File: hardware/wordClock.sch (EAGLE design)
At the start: 38 parts, among them J1 SPI_PRG, Q1 MOSFET-PCHANNELSMD, Q2 MOSFET-PCHANNELSMD, Q3 MOSFET-PCHANNELSMD, Q4 MOSFET-PCHANNELSMD, Q5 MOSFET-PCHANNELSMD, Q6 MOSFET-PCHANNELSMD, Q7 MOSFET-PCHANNELSMD, Q8 MOSFET-PCHANNELSMD, U2 TLC5940-NT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

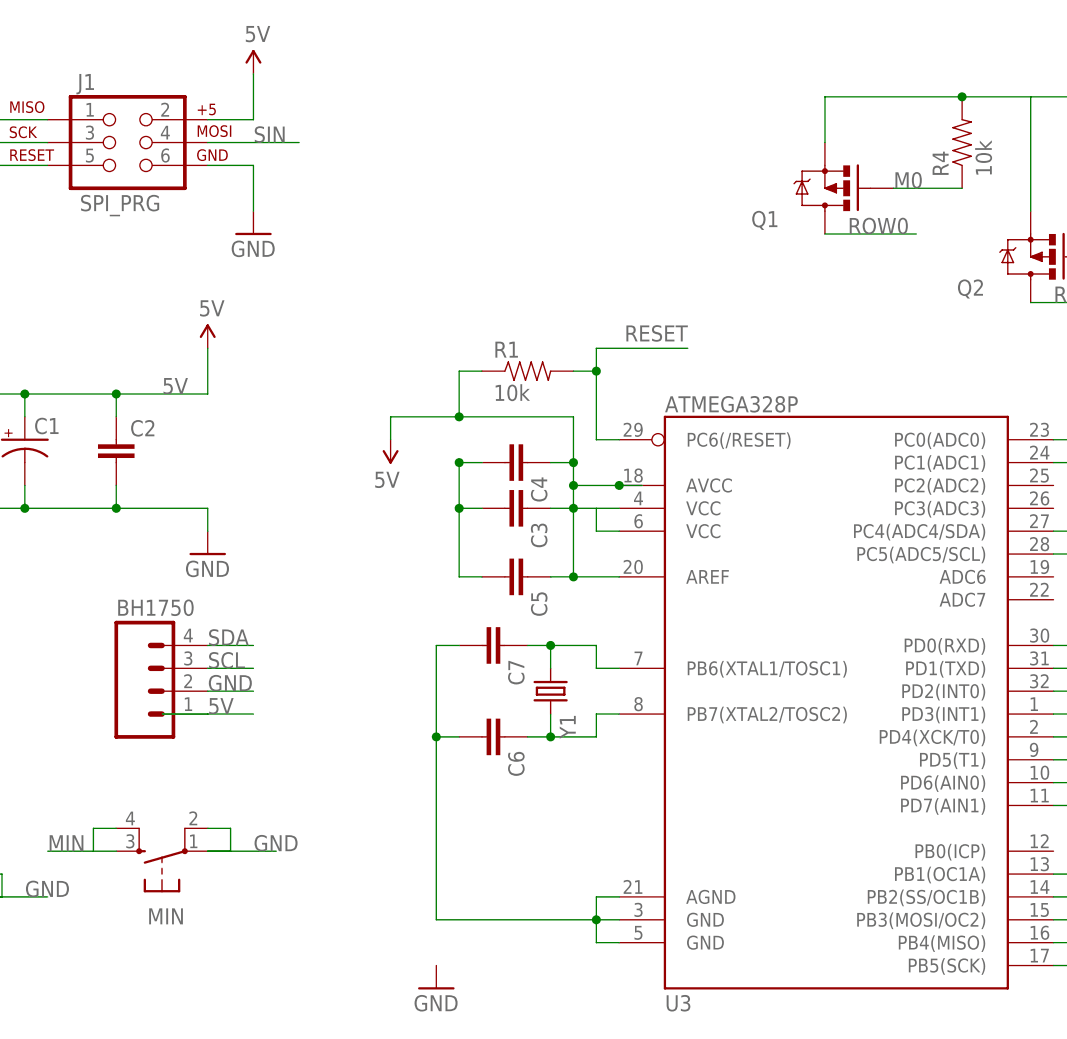
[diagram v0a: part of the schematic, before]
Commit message: Fixed floating nets.
Looks like the atmega got flipped and some nets were left floating.
Everything should be connected now.
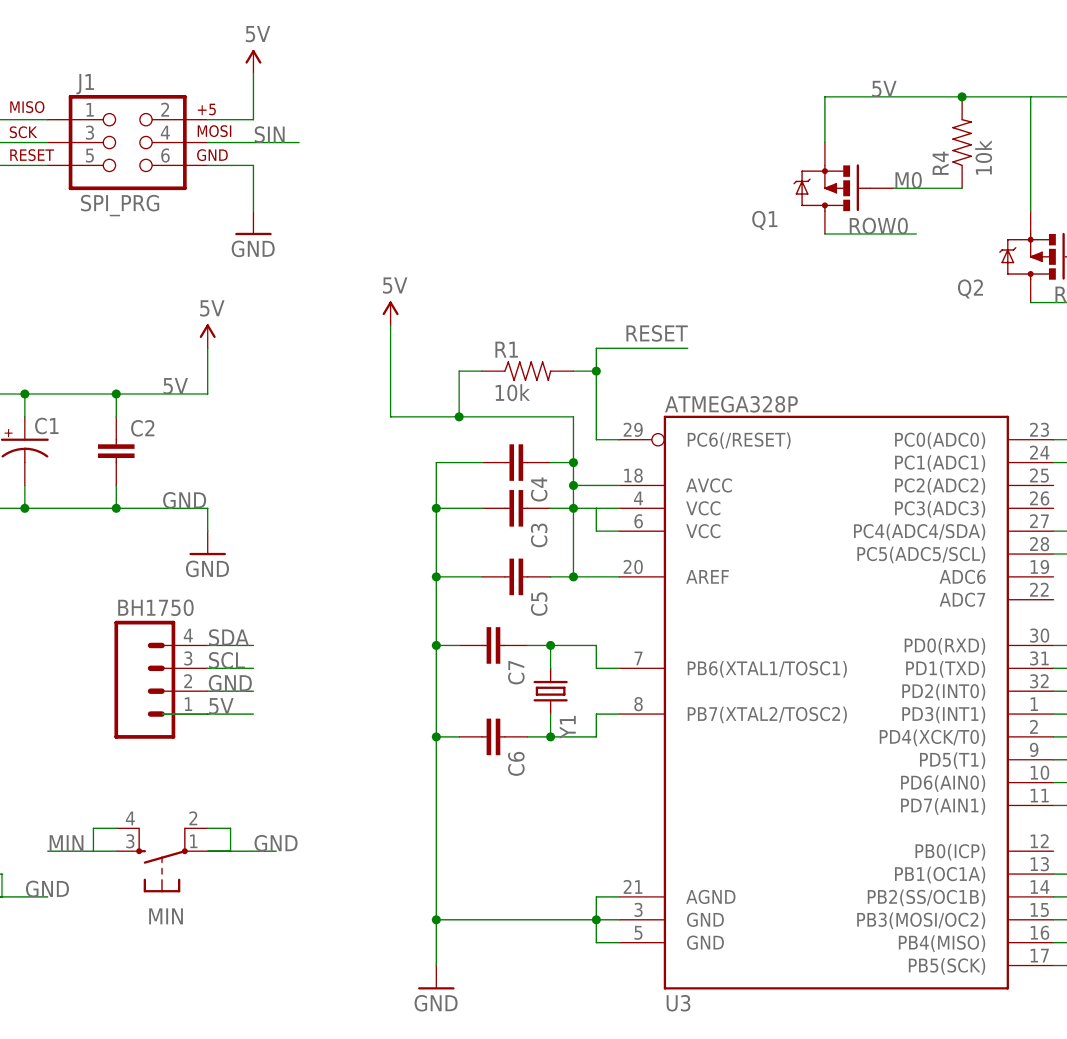
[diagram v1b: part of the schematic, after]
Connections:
- removed net N$3: C3.2, C4.2, C5.2
- removed net N$7: C6.2, C7.2, U3.AGND, U3.GND@1, U3.GND@2
- net GND: now also C3.2, C4.2, C5.2, C6.2, C7.2, U3.AGND, U3.GND@1, U3.GND@2
